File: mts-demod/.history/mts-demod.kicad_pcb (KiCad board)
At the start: 2 copper layers, 75.2 x 55 mm, 87 parts, among them IC1 ADE-1+, J1 RAW ERROR, J2 DEMOD IN, J3 DEMOD INPUT, J4 ANALOG ERROR, J5 PLP-5+, J6 INPUT PWR, U1 FDS010, U2 OPA858IDSGR, U3 OPA695IDR, U4 TCP-2-10X, U5 GVA-81, U6 0 dB atten, U7 PAT1220-C-4DB, U8 6 dB pad

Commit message: the most elegant board that i've ever laid out
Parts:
- added C40: 0.1u, Capacitor_SMD:C_0603_1608Metric, F.Cu at (172.9, 94.3)
- added C41: 0.1u, Capacitor_SMD:C_0603_1608Metric, F.Cu at (174.9, 94.3)
- added G***: LOGO, posm-logo:posm-logo-footprint, F.Cu at (141.2, 45.4)
- C18, C19, C21, C22, C23, C24: footprint Capacitor_SMD:C_0805_2012Metric -> Capacitor_SMD:C_0402_1005Metric
- TIA 1 OUT: renamed from TP2
- moved FB2 170.2 mm to (182.4, 90.0), turned to -90 degrees
- moved J3 164.8 mm to (180.0, 78.8)
- moved C37 157.0 mm to (180.2, 90.3), turned to 90 degrees
- moved C38 153.3 mm to (177.0, 91.0), turned to 180 degrees
- moved J2 153.0 mm to (167.6, 70.7), turned to 180 degrees
- moved U4 151.7 mm to (169.2, 80.9), turned to -90 degrees
- moved L2 149.2 mm to (157.3, 96.2)
- moved R16 147.7 mm to (186.8, 44.9)
- moved L1 145.3 mm to (168.4, 93.3), turned to 180 degrees
- moved L3 141.8 mm to (150.3, 96.1), turned to 180 degrees
- moved R13 138.1 mm to (169.3, 84.1), turned to 180 degrees
- moved J4 137.5 mm to (156.1, 67.8)
- moved R14 136.9 mm to (175.9, 44.9), turned to 180 degrees
- moved R15 136.9 mm to (175.9, 43.0), turned to 180 degrees
- moved C8 136.4 mm to (167.1, 50.6), turned to 90 degrees
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- renumbered D2 to +10V, D3 to +15V, D1 to +5V
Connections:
- C16 pad 1: Net-(C16-Pad1) -> CONN1
- C17 pad 1: Net-(C16-Pad1) -> CONN2
- J1 pad 3: (no net) -> GND
- J1 pad 4: (no net) -> GND
- J1 pad 5: (no net) -> GND
- J2 pad 3: (no net) -> GND
- J2 pad 4: (no net) -> GND
- J2 pad 5: (no net) -> GND
- J3 pad 3: (no net) -> GND
- J3 pad 4: (no net) -> GND
- J3 pad 5: (no net) -> GND
- J4 pad 3: (no net) -> GND
- J4 pad 4: (no net) -> GND
- J4 pad 5: (no net) -> GND
- U4 pad 2: Net-(C16-Pad1) -> CONN2
- U4 pad 5: Net-(C16-Pad1) -> CONN1
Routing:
- net Net-(C25-Pad2): track 0.00 -> 5.48 mm
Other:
- board size 75.2 x 55 mm -> 74.4 x 56.8 mm
- board text added: "10 MHz IN"
- board text added: "10 dB LO amplifier"
- board text added: "5 MHz LPF"
- board text added: "ADC CH.0"
- board text added: "ADC CH.1"
- board text added: "ANALOG ERROR"
- board text added: "FDS010"
- board text added: "J1"
- board text added: "J2"
- board text added: "J3"
- board text added: "J4"
- board text added: "PWR INPUT"
- board text added: "mts-demod v0"

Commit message: finished layout for demod
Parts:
- moved C13 2.97 mm to (148.5, 59.2), turned to 0 degrees
- moved TIA 1 OUT 1.64 mm to (160.1, 52.3)
- moved C38 1.56 mm to (178.4, 90.3), turned to 90 degrees
- moved C14 0.99 mm to (148.8, 60.6)
- moved G*** 0.75 mm to (141.2, 44.6)
- moved U6 0.66 mm to (173.2, 84.8)
- moved C6 0.57 mm to (162.6, 57.8)
- moved R13 0.22 mm to (169.2, 83.9)
- moved C19 0.21 mm to (130.1, 60.6)
- moved C9 0.15 mm to (167.1, 55.5)
- moved L3 0.15 mm to (150.3, 96.2)
- moved C23 0.15 mm to (130.1, 63.6)
- moved C18 0.15 mm to (135.1, 60.6)
- moved U7 0.15 mm to (146.1, 95.6)
- moved C28 0.12 mm to (154.0, 95.3)
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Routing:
- net +10V: track 0.00 -> 37.6 mm, vias 0 -> 3
- net INV_695: track 0.00 -> 18.6 mm, vias 0 -> 2
- net 25MHz_LPF2_OUT: track 0.00 -> 18.5 mm
- net 25MHz_LPF1: track 0.00 -> 17.0 mm
- net +5VA: track 0.00 -> 10.2 mm, vias 0 -> 5
- net ADC_CH1: track 0.00 -> 10.2 mm
- net DEMOD_IF: track 0.00 -> 9.73 mm
- net 10MHz_DEMOD_IN: track 0.00 -> 8.90 mm
- net V_REF: track 0.00 -> 8.68 mm
- net OUT_695: track 0.00 -> 7.95 mm
- net ADC_CH0: track 0.00 -> 7.86 mm
- net ADC_CH1b: track 0.00 -> 7.73 mm
- net 25MHz_LPF2: track 0.00 -> 7.42 mm
- net FDS010_ANODE: track 0.00 -> 7.18 mm
- net Net-(D2-K): track 0.00 -> 6.37 mm
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- added copper zone on B.Cu, net +15V
- added copper zone on F.Cu, net +15V
- added copper zone on In2.Cu, net +15V
- added copper zone on B.Cu, net +5V
- added copper zone on F.Cu, net +5V
- added copper zone on In2.Cu, net +5V
- added copper zone on F.Cu, net +5VA
- added copper zone on In2.Cu, net +5VA
- added copper zone on F.Cu, net +5VA_GVA
- added copper zone on F.Cu, net GND
- added copper zone on In1.Cu, net GND
- added copper zone on In2.Cu, net GND
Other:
- board size 74.4 x 56.8 mm -> 74.4 x 57.3 mm
- copper layers 2 -> 4

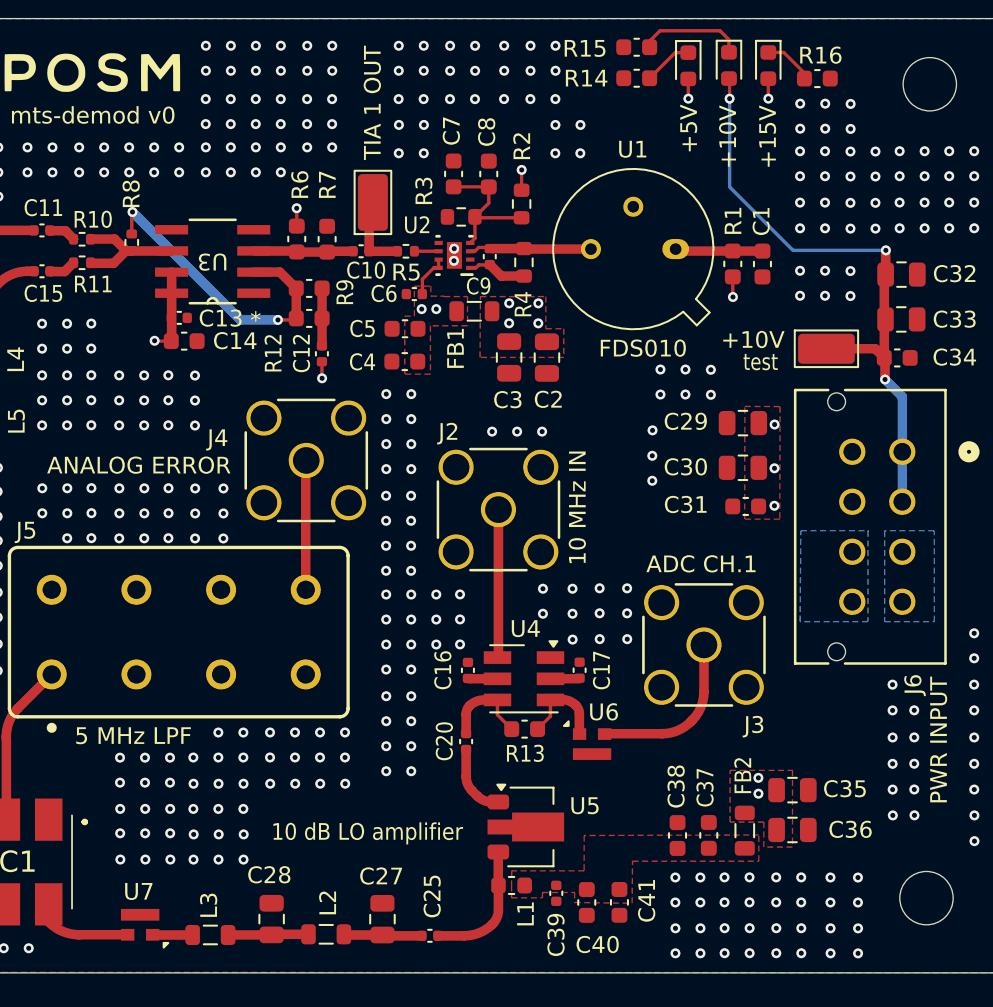
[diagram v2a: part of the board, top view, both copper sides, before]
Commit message: added more stitch and thermals
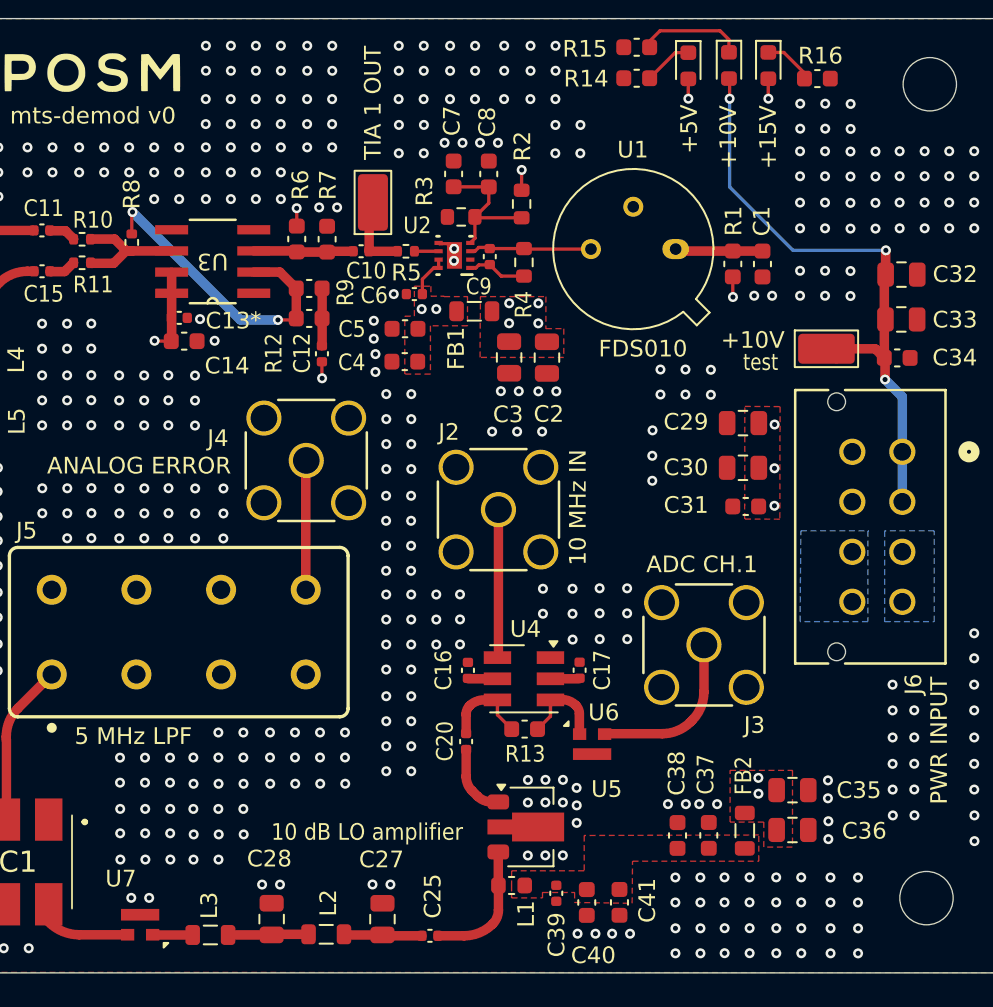
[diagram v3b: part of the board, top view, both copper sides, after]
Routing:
- net GND: track 6.36 -> 7.44 mm, vias 464 -> 518
